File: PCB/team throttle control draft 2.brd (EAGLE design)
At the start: 75.9 x 59.7 mm, 15 parts, among them IC1 ICL7663CPA, IC4 7805T

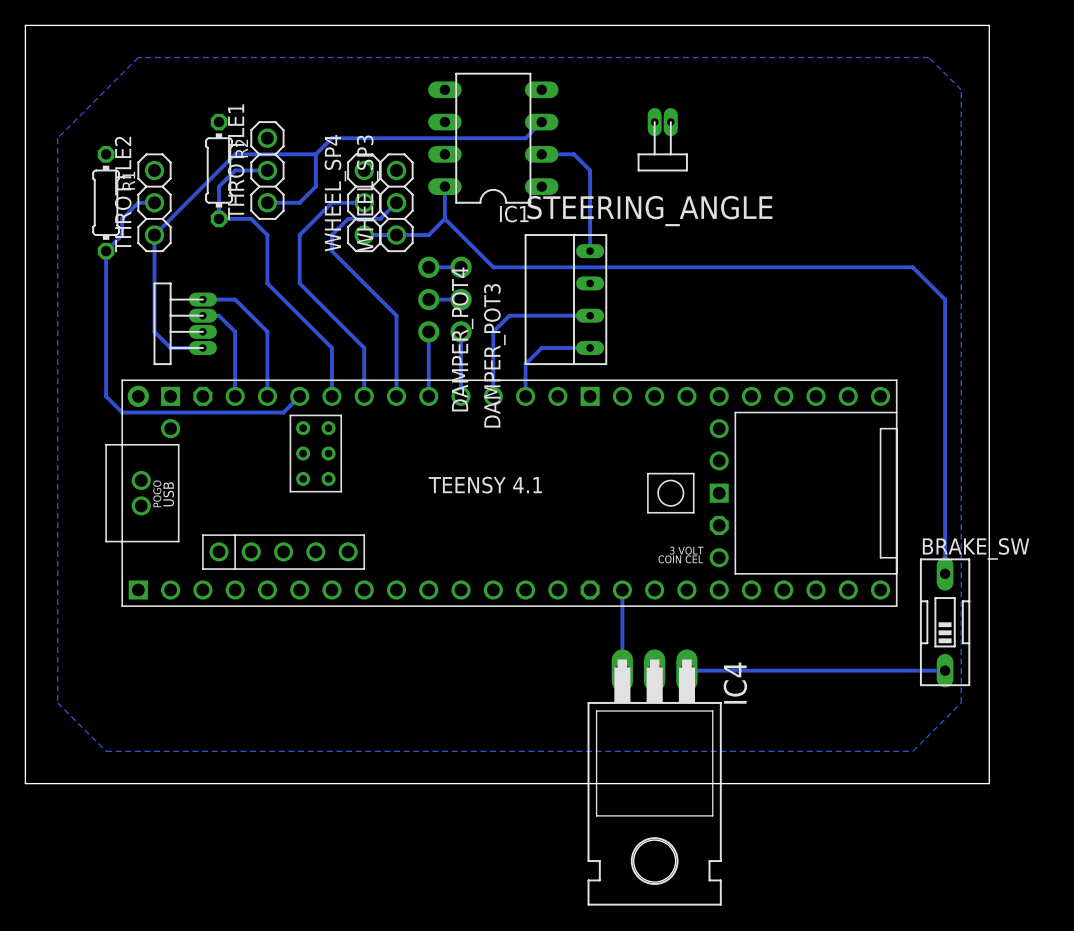
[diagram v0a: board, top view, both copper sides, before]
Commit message: Dump car_software's PCB folder into new repository.
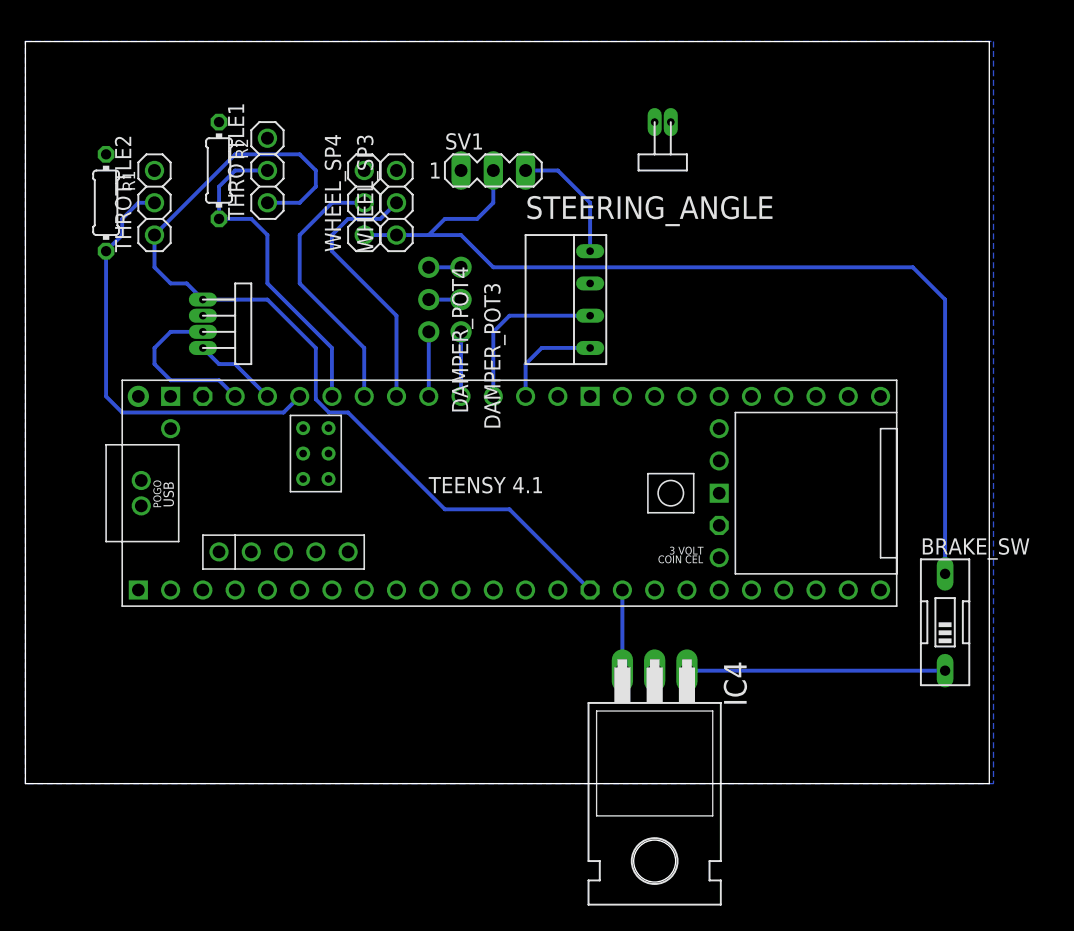
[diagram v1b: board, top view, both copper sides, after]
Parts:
- removed IC1: ICL7663CPA, maxim:DIL08
- added SV1: (no value), con-lstb:MA03-1
- moved U$11 9.25 mm to (36.8, 61.0), turned to 270 degrees
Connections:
- net 12V: now also SV1.2; no longer IC1.8
- net 3.3V: now also U$3.3V3-1; no longer IC1.3
- net 5V: now also SV1.3; no longer IC1.2
- net GND: now also SV1.1; no longer IC1.4
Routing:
- net 3.3V: track 53.0 -> 71.2 mm
- net 12V: track 73.0 -> 78.1 mm
- net CRX_2: track 8.15 -> 13.0 mm
- net CTX_2: track 11.2 -> 6.66 mm
- net 5V: track 10.7 -> 9.94 mm
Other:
- board size 75.9 x 59.7 mm -> 75.9 x 58.4 mm
